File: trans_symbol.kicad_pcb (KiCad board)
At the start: 2 copper layers, 95.9 x 84.7 mm, 48 parts, among them J3 USB_B_Micro, U1 ATSAMD21G18A-AU, U2 MIC5504-3.3YM5, Y1 32768Hz

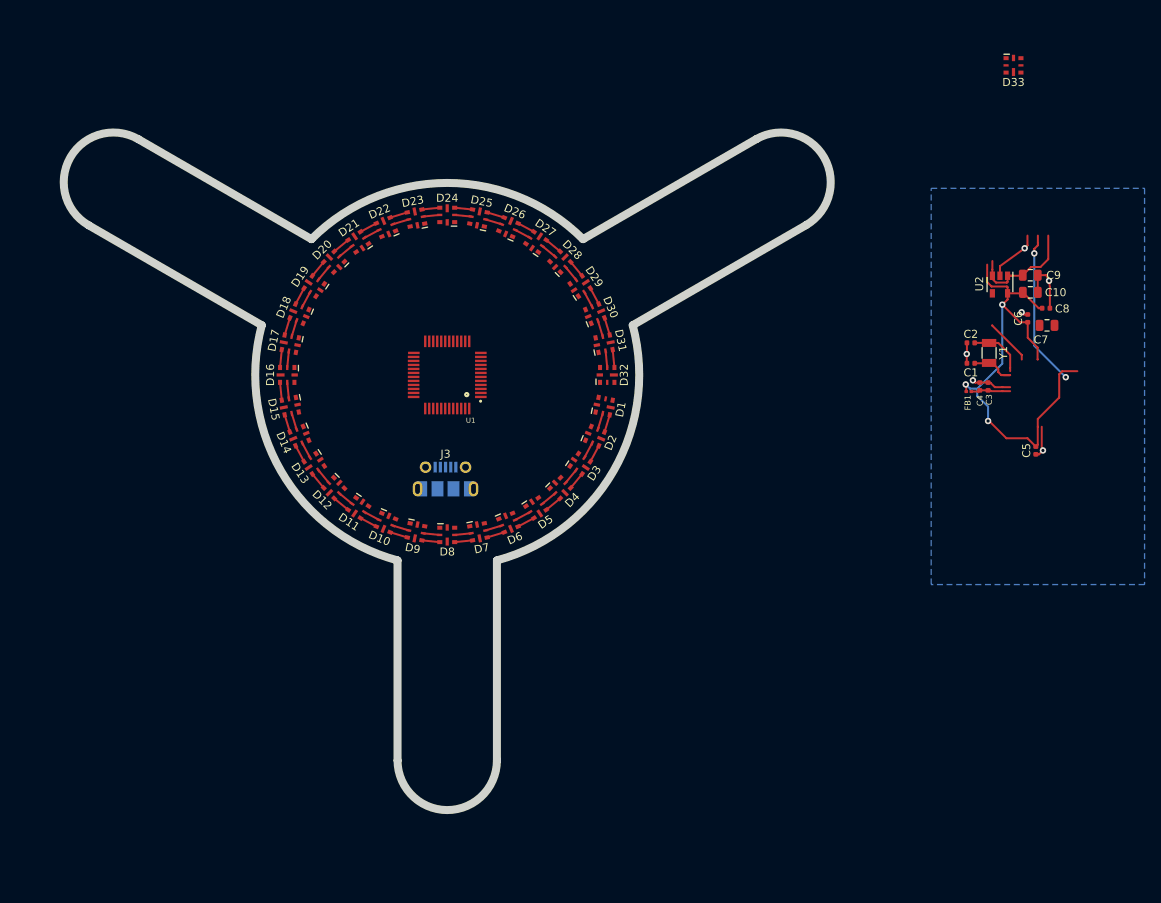
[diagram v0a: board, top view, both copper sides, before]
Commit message: fix spokes to match the non-uniform spacing that the symbol apparently has
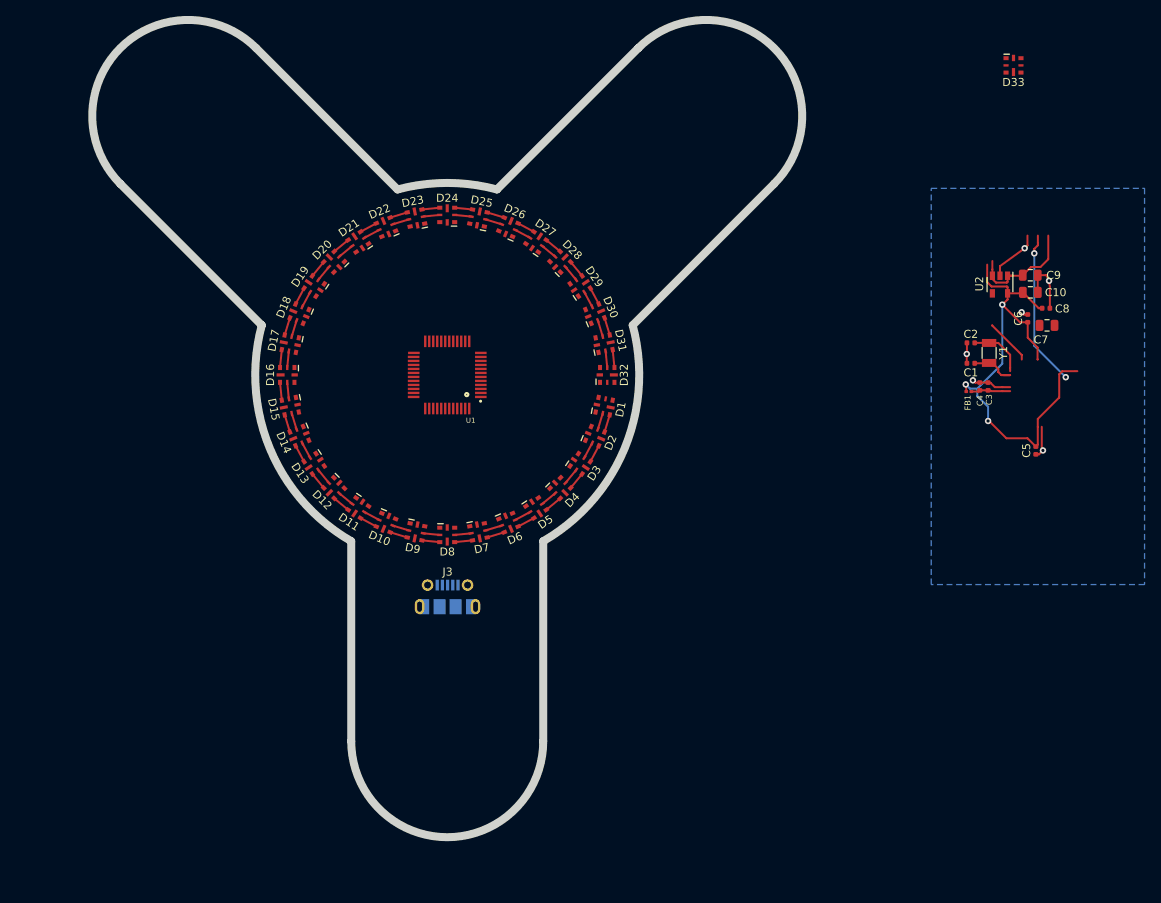
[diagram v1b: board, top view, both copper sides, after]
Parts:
- moved J3 14.7 mm to (90.0, 117.7)
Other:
- board size 95.9 x 84.7 mm -> 88.7 x 102.2 mm
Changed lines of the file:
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@@
   )
   (module Connector_USB:USB_Micro-B_Molex-105017-0001 (layer B.Cu)
-    (at 89.789 102.997 180)
+    (at 90.043 117.729 180)
     (descr http://www.molex.com/pdm_docs/sd/1050170001_sd.pdf)
     (tags "Micro-USB SMD Typ-B")
@@
     )
   )
-  (gr_arc (start 131.727026 65.90889) (end 128.621197 60.529437) (angle 180) (layer Edge.Cuts) (width 1))
-  (gr_line (start 113.182219 83.788342) (end 134.832854 71.288342) (layer Edge.Cuts) (width 1))
-  (gr_line (start 106.970562 73.029437) (end 128.621197 60.529437) (layer Edge.Cuts) (width 1))
-  (gr_arc (start 90 90) (end 73.029437 73.029437) (angle 90) (layer Edge.Cuts) (width 1))
-  (gr_arc (start 48.272973 65.90889) (end 45.167145 71.288342) (angle 180) (layer Edge.Cuts) (width 1))
-  (gr_line (start 73.029437 73.029437) (end 51.378802 60.529437) (layer Edge.Cuts) (width 1))
-  (gr_line (start 66.81778 83.788342) (end 45.167145 71.288342) (layer Edge.Cuts) (width 1))
-  (gr_arc (start 90 90) (end 83.788342 113.182219) (angle 90) (layer Edge.Cuts) (width 1))
-  (gr_arc (start 90 138.182219) (end 96.211657 138.182219) (angle 180) (layer Edge.Cuts) (width 1))
-  (gr_line (start 83.788342 113.182219) (end 83.788342 138.182219) (layer Edge.Cuts) (width 1))
-  (gr_line (start 96.211657 113.182219) (end 96.211657 138.182219) (layer Edge.Cuts) (width 1))
-  (gr_arc (start 90 90) (end 113.182219 83.788342) (angle 90) (layer Edge.Cuts) (width 1))
+  (gr_arc (start 90 135.784609) (end 102 135.784609) (angle 180) (layer Edge.Cuts) (width 1))
+  (gr_line (start 78 110.784609) (end 78 135.784609) (layer Edge.Cuts) (width 1))
+  (gr_line (start 102 110.784609) (end 102 135.784609) (layer Edge.Cuts) (width 1))
+  (gr_arc (start 90 90) (end 113.182219 83.788342) (angle 75) (layer Edge.Cuts) (width 1))
+  (gr_arc (start 122.374607 57.625392) (end 113.889326 49.14011) (angle 180) (layer Edge.Cuts) (width 1))
+  (gr_line (start 113.182219 83.788342) (end 130.859889 66.110673) (layer Edge.Cuts) (width 1))
+  (gr_line (start 96.211657 66.81778) (end 113.889326 49.14011) (layer Edge.Cuts) (width 1))
+  (gr_arc (start 90 90) (end 83.788342 66.81778) (angle 30) (layer Edge.Cuts) (width 1))
+  (gr_arc (start 57.625392 57.625392) (end 49.14011 66.110673) (angle 180) (layer Edge.Cuts) (width 1))
+  (gr_line (start 83.788342 66.81778) (end 66.110673 49.14011) (layer Edge.Cuts) (width 1))
+  (gr_line (start 66.81778 83.788342) (end 49.14011 66.110673) (layer Edge.Cuts) (width 1))
+  (gr_arc (start 90 90) (end 78 110.784609) (angle 75) (layer Edge.Cuts) (width 1))
   (via (at 154.94 87.376) (size 0.8) (drill 0.4) (layers F.Cu B.Cu) (net 1))
   (segment (start 163.815 79.6671) (end 163.8277 79.6798) (width 0.25) (layer F.Cu) (net 1))

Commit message: start working on spokes
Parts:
- added D34: APA102-2020, LED_SMD:LED-APA102-2020_tightened_pads, F.Cu at (116.5, 63.5)
- added D35: APA102-2020, LED_SMD:LED-APA102-2020_tightened_pads, F.Cu at (119.0, 61.0)
- added D36: APA102-2020, LED_SMD:LED-APA102-2020_tightened_pads, F.Cu at (121.5, 58.5)
- added D37: APA102-2020, LED_SMD:LED-APA102-2020_tightened_pads, F.Cu at (123.9, 56.1)
- added D38: APA102-2020, LED_SMD:LED-APA102-2020_tightened_pads, F.Cu at (106.0, 77.9)
- added D39: APA102-2020, LED_SMD:LED-APA102-2020_tightened_pads, F.Cu at (107.9, 81.1)
- added D40: APA102-2020, LED_SMD:LED-APA102-2020_tightened_pads, F.Cu at (109.2, 84.5)
- added D41: APA102-2020, LED_SMD:LED-APA102-2020_tightened_pads, F.Cu at (109.9, 88.2)
- added D42: APA102-2020, LED_SMD:LED-APA102-2020_tightened_pads, F.Cu at (109.9, 91.8)
- added D43: APA102-2020, LED_SMD:LED-APA102-2020_tightened_pads, F.Cu at (109.2, 95.5)
- added D44: APA102-2020, LED_SMD:LED-APA102-2020_tightened_pads, F.Cu at (107.9, 98.9)
- added D45: APA102-2020, LED_SMD:LED-APA102-2020_tightened_pads, F.Cu at (106.0, 102.1)
- added D46: APA102-2020, LED_SMD:LED-APA102-2020_tightened_pads, F.Cu at (103.5, 104.8)
- added D47: APA102-2020, LED_SMD:LED-APA102-2020_tightened_pads, F.Cu at (100.5, 107.0)
- added D48: APA102-2020, LED_SMD:LED-APA102-2020_tightened_pads, F.Cu at (97.2, 108.6)
- added D49: APA102-2020, LED_SMD:LED-APA102-2020_tightened_pads, F.Cu at (93.7, 109.7)
- added D50: APA102-2020, LED_SMD:LED-APA102-2020_tightened_pads, F.Cu at (90.0, 113.5)
- added D51: APA102-2020, LED_SMD:LED-APA102-2020_tightened_pads, F.Cu at (90.0, 117.0)
- added D52: APA102-2020, LED_SMD:LED-APA102-2020_tightened_pads, F.Cu at (90.0, 120.5)
- added D53: APA102-2020, LED_SMD:LED-APA102-2020_tightened_pads, F.Cu at (90.0, 124.0)
- added D54: APA102-2020, LED_SMD:LED-APA102-2020_tightened_pads, F.Cu at (90.0, 127.5)
- added D55: APA102-2020, LED_SMD:LED-APA102-2020_tightened_pads, F.Cu at (90.0, 131.0)
- added D56, D59: APA102-2020, LED_SMD:LED-APA102-2020_tightened_pads, F.Cu at (90.0, 134.5)
- added D57, D60: APA102-2020, LED_SMD:LED-APA102-2020_tightened_pads, F.Cu at (90.0, 138.0)
- added D58, D61: APA102-2020, LED_SMD:LED-APA102-2020_tightened_pads, F.Cu at (90.0, 110.0)
- added D62: APA102-2020, LED_SMD:LED-APA102-2020_tightened_pads, F.Cu at (68.1, 122.8)
- added D63: APA102-2020, LED_SMD:LED-APA102-2020_tightened_pads, F.Cu at (64.1, 127.1)
- added D64: APA102-2020, LED_SMD:LED-APA102-2020_tightened_pads, F.Cu at (68.1, 127.1)
- added D65: APA102-2020, LED_SMD:LED-APA102-2020_tightened_pads, F.Cu at (37.8, 138.2)
- added D66: APA102-2020, LED_SMD:LED-APA102-2020_tightened_pads, F.Cu at (37.8, 142.4)
- added D67: APA102-2020, LED_SMD:LED-APA102-2020_tightened_pads, F.Cu at (41.9, 138.2)
- added D68: APA102-2020, LED_SMD:LED-APA102-2020_tightened_pads, F.Cu at (37.8, 146.6)
- added D69: APA102-2020, LED_SMD:LED-APA102-2020_tightened_pads, F.Cu at (45.9, 138.2)
- added D70: APA102-2020, LED_SMD:LED-APA102-2020_tightened_pads, F.Cu at (41.9, 142.4)
- added D71: APA102-2020, LED_SMD:LED-APA102-2020_tightened_pads, F.Cu at (37.8, 150.8)
- added D72: APA102-2020, LED_SMD:LED-APA102-2020_tightened_pads, F.Cu at (45.9, 142.4)
- added D73: APA102-2020, LED_SMD:LED-APA102-2020_tightened_pads, F.Cu at (41.9, 146.6)
- added D74: APA102-2020, LED_SMD:LED-APA102-2020_tightened_pads, F.Cu at (50.0, 138.2)
- added D75: APA102-2020, LED_SMD:LED-APA102-2020_tightened_pads, F.Cu at (54.0, 138.2)
- added D76: APA102-2020, LED_SMD:LED-APA102-2020_tightened_pads, F.Cu at (50.0, 142.4)
- added D77: APA102-2020, LED_SMD:LED-APA102-2020_tightened_pads, F.Cu at (45.9, 146.6)
- added D78: APA102-2020, LED_SMD:LED-APA102-2020_tightened_pads, F.Cu at (41.9, 150.8)
- added D79: APA102-2020, LED_SMD:LED-APA102-2020_tightened_pads, F.Cu at (54.0, 142.4)
- added D80: APA102-2020, LED_SMD:LED-APA102-2020_tightened_pads, F.Cu at (58.1, 138.2)
- added D81: APA102-2020, LED_SMD:LED-APA102-2020_tightened_pads, F.Cu at (50.0, 146.6)
- added D82: APA102-2020, LED_SMD:LED-APA102-2020_tightened_pads, F.Cu at (45.9, 150.8)
- added D83: APA102-2020, LED_SMD:LED-APA102-2020_tightened_pads, F.Cu at (54.0, 146.6)
- added D84: APA102-2020, LED_SMD:LED-APA102-2020_tightened_pads, F.Cu at (62.1, 138.2)
- added D85: APA102-2020, LED_SMD:LED-APA102-2020_tightened_pads, F.Cu at (58.1, 142.4)
- added D86: APA102-2020, LED_SMD:LED-APA102-2020_tightened_pads, F.Cu at (50.0, 150.8)
- added D87: APA102-2020, LED_SMD:LED-APA102-2020_tightened_pads, F.Cu at (54.0, 150.8)
- added D88: APA102-2020, LED_SMD:LED-APA102-2020_tightened_pads, F.Cu at (62.1, 142.4)
- added D89: APA102-2020, LED_SMD:LED-APA102-2020_tightened_pads, F.Cu at (58.1, 146.6)
- added D90: APA102-2020, LED_SMD:LED-APA102-2020_tightened_pads, F.Cu at (66.2, 138.2)
- added D91: APA102-2020, LED_SMD:LED-APA102-2020_tightened_pads, F.Cu at (66.2, 142.4)
- added D92: APA102-2020, LED_SMD:LED-APA102-2020_tightened_pads, F.Cu at (62.1, 146.6)
- added D93: APA102-2020, LED_SMD:LED-APA102-2020_tightened_pads, F.Cu at (58.1, 150.8)
- added D94: APA102-2020, LED_SMD:LED-APA102-2020_tightened_pads, F.Cu at (66.2, 146.6)
- added D95: APA102-2020, LED_SMD:LED-APA102-2020_tightened_pads, F.Cu at (62.1, 150.8)
- added D96: APA102-2020, LED_SMD:LED-APA102-2020_tightened_pads, F.Cu at (66.2, 150.8)
- D33: value LED-APA102-2020 -> APA102-2020
- moved D33 49.0 mm to (114.0, 66.0), turned to 225 degrees
- moved C1 31.6 mm to (134.1, 111.9)
- moved C2 31.6 mm to (134.1, 109.4)
- moved C3 31.6 mm to (136.3, 114.8)
- moved C6 31.6 mm to (141.2, 106.3)
- moved Y1 31.6 mm to (136.4, 110.6)
- moved C7 31.6 mm to (143.6, 107.2)
- moved C8 31.6 mm to (143.5, 105.0)
- moved C4 31.6 mm to (135.2, 114.8)
- moved U2 31.6 mm to (137.8, 102.1)
- moved C10 31.6 mm to (141.6, 103.0)
- moved C5 31.6 mm to (142.2, 122.8)
- moved C9 31.6 mm to (141.5, 100.9)
- moved FB1 31.6 mm to (133.9, 115.4)
- moved D1 28.1 mm to (86.3, 109.7), turned to 349.412 degrees
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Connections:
- net /Sheet5F81AC31/SCK renamed /Sheet5F81AC31/LED_SCK
- net /Sheet5F81AC31/SDO renamed /Sheet5F81AC31/LED_DATA
- D32 pad 2: Net-(D32-Pad2) -> D32_CKO
- D32 pad 3: Net-(D32-Pad3) -> D32_SDO
- D33 pad 1: (no net) -> +5V
- D33 pad 2: (no net) -> Net-(D33-Pad2)
- D33 pad 3: (no net) -> Net-(D33-Pad3)
- D33 pad 4: (no net) -> D32_SDO
- D33 pad 5: (no net) -> D32_CKO
- D33 pad 6: (no net) -> GND
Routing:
- net Net-(D37-Pad2): track 0.00 -> 29.1 mm
- net Net-(D57-Pad2): track 0.00 -> 28.9 mm
- net Net-(D37-Pad3): track 0.00 -> 28.2 mm
- net Net-(D57-Pad3): track 0.00 -> 28.0 mm
- net Net-(D49-Pad2): track 0.00 -> 3.89 mm
- net Net-(D49-Pad3): track 0.00 -> 2.75 mm
- net Net-(D20-Pad3): track 2.25 -> 0.00 mm
- net Net-(D20-Pad2): track 2.07 -> 0.00 mm
- net Net-(D41-Pad3): track 0.00 -> 2.00 mm
- net Net-(D45-Pad3): track 0.00 -> 2.00 mm
- net Net-(D43-Pad3): track 0.00 -> 2.00 mm
- net Net-(D39-Pad3): track 0.00 -> 2.00 mm
- net Net-(D47-Pad3): track 0.00 -> 2.00 mm
- net Net-(D42-Pad3): track 0.00 -> 2.00 mm
- net Net-(D40-Pad3): track 0.00 -> 2.00 mm
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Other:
- board size 88.7 x 102.2 mm -> 81.7 x 93.6 mm
- board text added: "Do I wanna use an ATSAMD21E18A instead?"
- board text added: "sercom1"
- board text added: "sercom3/sda/scl"
- board text added: "sercom4"
- board text added: "sercom5"
- board text added: "sercom5 (pick)"

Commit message: clean up various point-like object types; tweak Edge.Cuts to be precise overlap in order to fix pcbnew thinking it wasn't a closed shape, but turns out this was also a bug fixed in kicad-5.1.3 so I'm not sure if this change was actually necessary, but it works now
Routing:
- net Net-(D20-Pad2): track 0.00 -> 28.9 mm
- net Net-(D20-Pad3): track 0.00 -> 28.0 mm

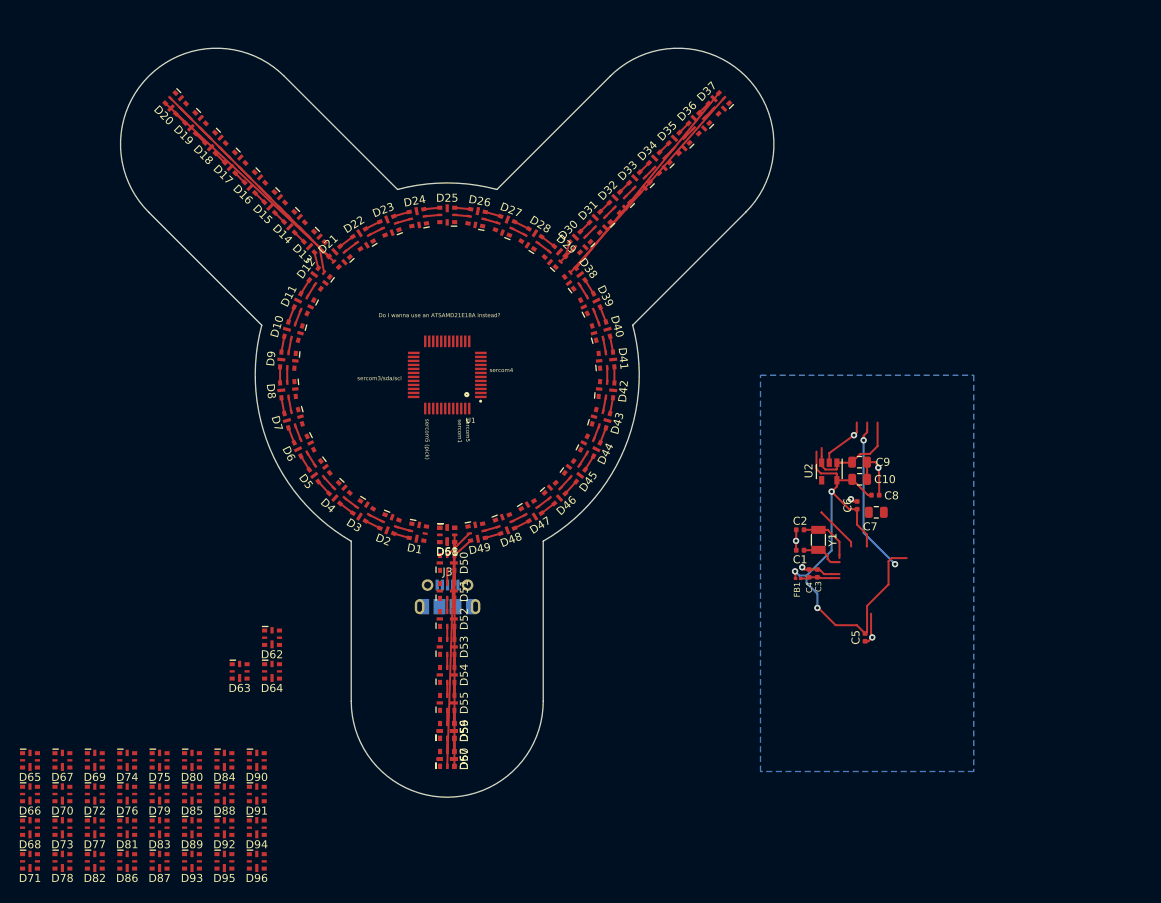
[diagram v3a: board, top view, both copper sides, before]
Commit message: first pass on complete trans symbol
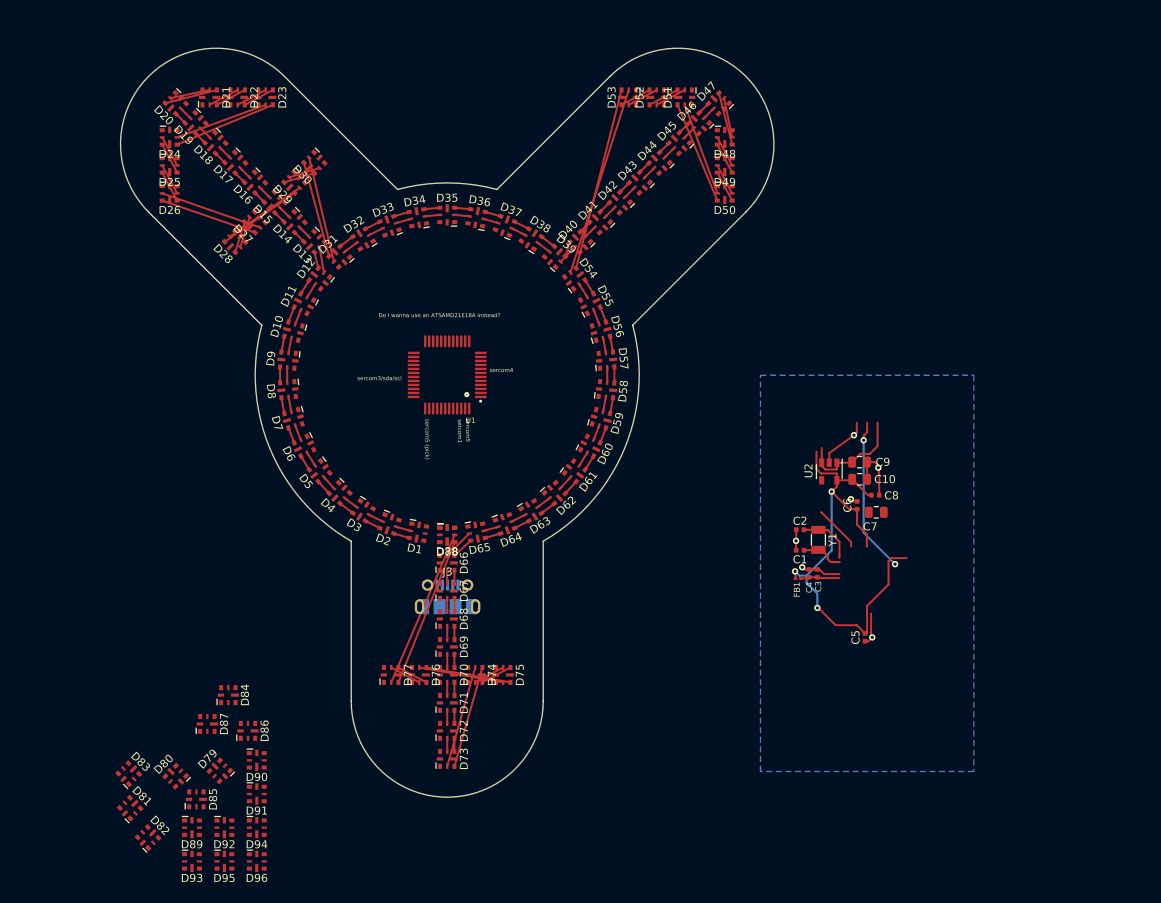
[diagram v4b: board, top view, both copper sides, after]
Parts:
- moved D53 72.3 mm to (112.7, 55.3), turned to 270 degrees
- moved D52 70.3 mm to (116.2, 55.3), turned to 270 degrees
- moved D51 68.5 mm to (119.7, 55.3), turned to 270 degrees
- moved D78 63.1 mm to (90.0, 110.0)
- moved D65 62.7 mm to (93.7, 109.7), turned to 10.5882 degrees
- moved D66 59.6 mm to (90.0, 113.5), turned to 90 degrees
- moved D68 58.3 mm to (90.0, 120.5), turned to 90 degrees
- moved D50 57.8 mm to (124.7, 67.3), turned to 0 degrees
- moved D47 56.1 mm to (123.9, 56.1), turned to 225 degrees
- moved D71 55.8 mm to (90.0, 131.0), turned to 90 degrees
- moved D48 55.6 mm to (124.7, 60.3), turned to 0 degrees
- moved D49 55.4 mm to (124.7, 63.8), turned to 0 degrees
- moved D57 53.7 mm to (109.9, 88.2), turned to 95.2941 degrees
- moved D56 53.5 mm to (109.2, 84.5), turned to 105.882 degrees
- moved D55 53.0 mm to (107.9, 81.1), turned to 116.471 degrees
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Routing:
- net Net-(D37-Pad2): track 29.1 -> 1.84 mm
- net Net-(D57-Pad2): track 28.9 -> 1.84 mm
- net Net-(D37-Pad3): track 28.2 -> 2.00 mm
- net Net-(D57-Pad3): track 28.0 -> 2.00 mm
- net Net-(D20-Pad2): track 28.9 -> 5.01 mm
- net Net-(D53-Pad2): track 1.64 -> 24.0 mm
- net Net-(D20-Pad3): track 28.0 -> 6.65 mm
- net Net-(D53-Pad3): track 1.64 -> 23.0 mm
- net Net-(D77-Pad2): track 0.00 -> 20.1 mm
- net Net-(D77-Pad3): track 0.00 -> 18.9 mm
- net Net-(D73-Pad3): track 0.00 -> 12.8 mm
- net Net-(D73-Pad2): track 0.00 -> 12.8 mm
- net Net-(D30-Pad2): track 1.64 -> 13.4 mm
- net Net-(D50-Pad3): track 1.64 -> 13.0 mm
- net Net-(D26-Pad2): track 1.84 -> 13.0 mm
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
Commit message: flip arrow without cross to save a via
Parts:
- moved D50 17.0 mm to (112.7, 55.3), turned to 270 degrees
- moved D53 17.0 mm to (124.7, 67.3), turned to 0 degrees
- moved D49 12.0 mm to (116.2, 55.3), turned to 270 degrees
- moved D52 12.0 mm to (124.7, 63.8), turned to 0 degrees
- moved D48 7.07 mm to (119.7, 55.3), turned to 270 degrees
- moved D51 7.07 mm to (124.7, 60.3), turned to 0 degrees
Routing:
- net Net-(D53-Pad3): track 23.0 -> 19.6 mm
- net Net-(D53-Pad2): track 24.0 -> 20.9 mm
- net Net-(D50-Pad3): track 13.0 -> 15.4 mm
- net Net-(D50-Pad2): track 11.8 -> 14.2 mm
- net Net-(D47-Pad3): track 6.65 -> 5.38 mm

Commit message: fix pixel orientation on arrow & cross
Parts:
- turned D21 to 0 degrees
- turned D22 to 0 degrees
- turned D23 to 0 degrees
- turned D24 to 270 degrees
- turned D25 to 270 degrees
- turned D26 to 270 degrees
- turned D27 to 45 degrees
- turned D28 to 45 degrees
- turned D29 to 225 degrees
- turned D30 to 225 degrees
- turned D48 to 180 degrees
- turned D49 to 180 degrees
- turned D50 to 180 degrees
- turned D51 to 270 degrees
- turned D52 to 270 degrees
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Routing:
- net Net-(D50-Pad3): track 15.4 -> 12.3 mm
- net Net-(D76-Pad3): track 3.96 -> 1.64 mm
- net Net-(D76-Pad2): track 3.96 -> 1.64 mm
- net Net-(D74-Pad3): track 3.96 -> 1.64 mm
- net Net-(D74-Pad2): track 3.96 -> 1.64 mm
- net Net-(D27-Pad3): track 3.96 -> 1.64 mm
- net Net-(D29-Pad2): track 3.96 -> 1.64 mm
- net Net-(D27-Pad2): track 3.96 -> 1.64 mm
- net Net-(D29-Pad3): track 3.96 -> 1.64 mm
- net Net-(D50-Pad2): track 14.2 -> 12.6 mm
- net Net-(D49-Pad3): track 3.96 -> 5.36 mm
- net Net-(D49-Pad2): track 3.96 -> 5.36 mm
- net Net-(D48-Pad3): track 3.96 -> 5.36 mm
- net Net-(D48-Pad2): track 3.96 -> 5.36 mm
- net Net-(D51-Pad3): track 3.96 -> 5.36 mm
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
